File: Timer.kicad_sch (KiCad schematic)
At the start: 26 parts, among them J201 Conn_02x06_Row_Letter_First, P201 Interrupt Daisy Chain SIO, P202 Interrupt Daisy Chain CTC, P203 CONN_02X10, P204 Outputs, P205 Inputs, U201 Z8430, U202 Z8440

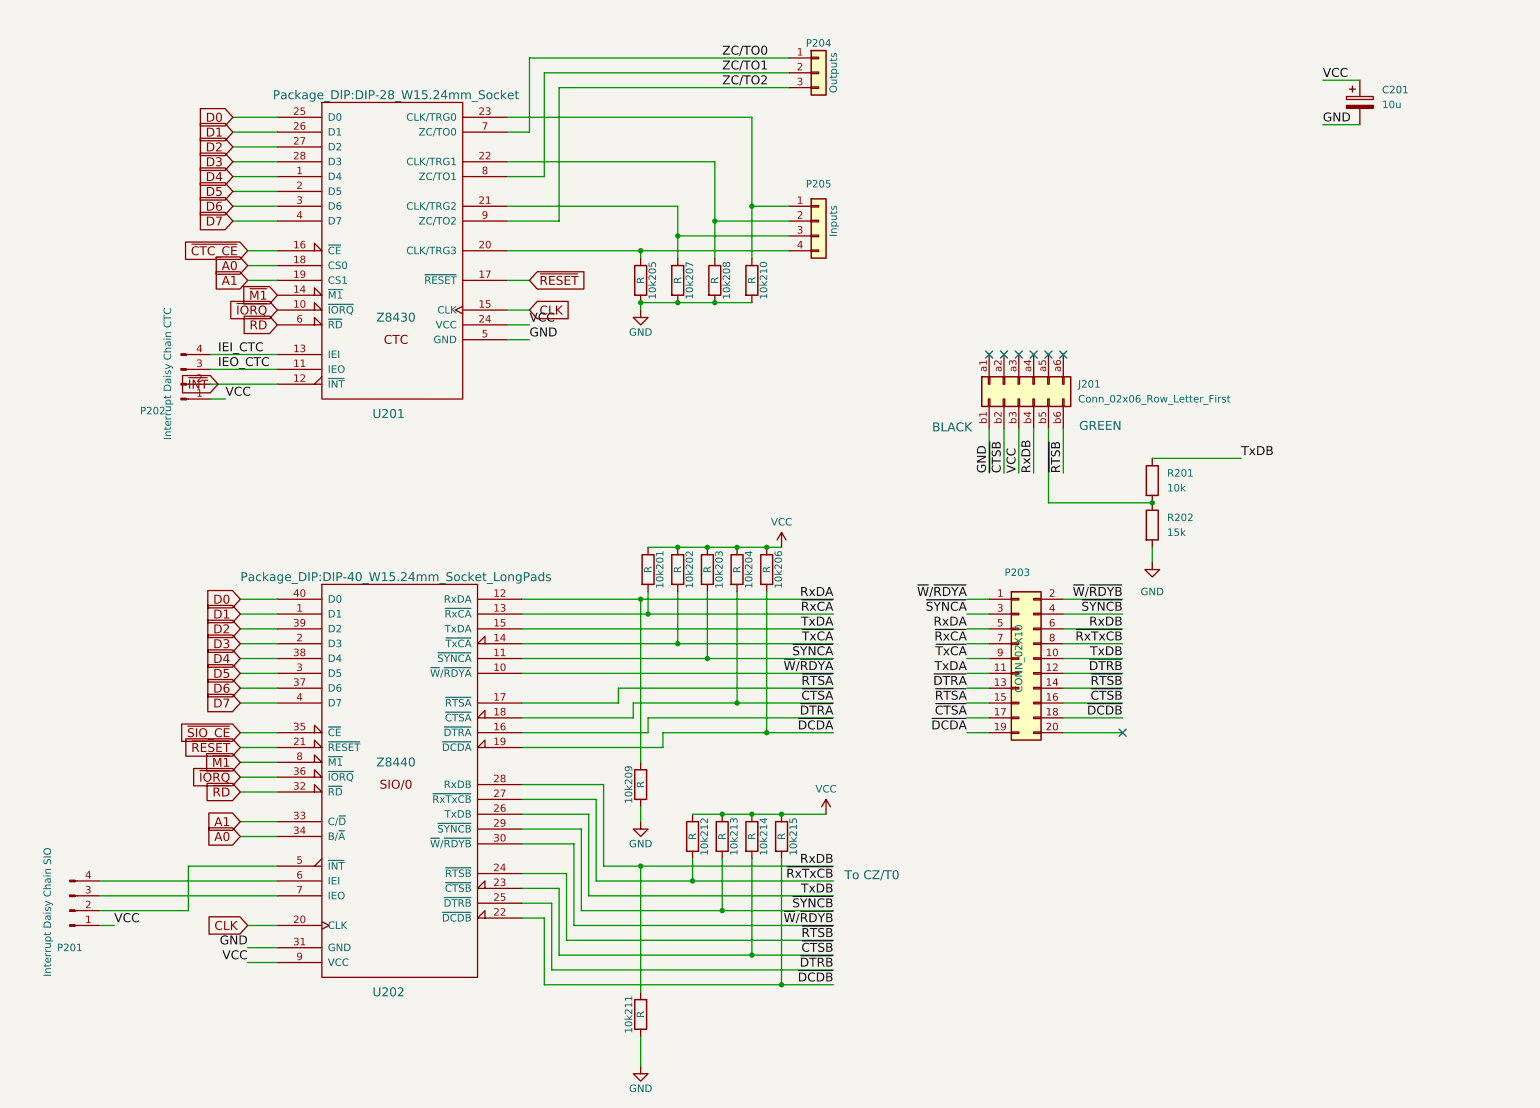
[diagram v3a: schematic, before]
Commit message: Continued layout of timer/sio board
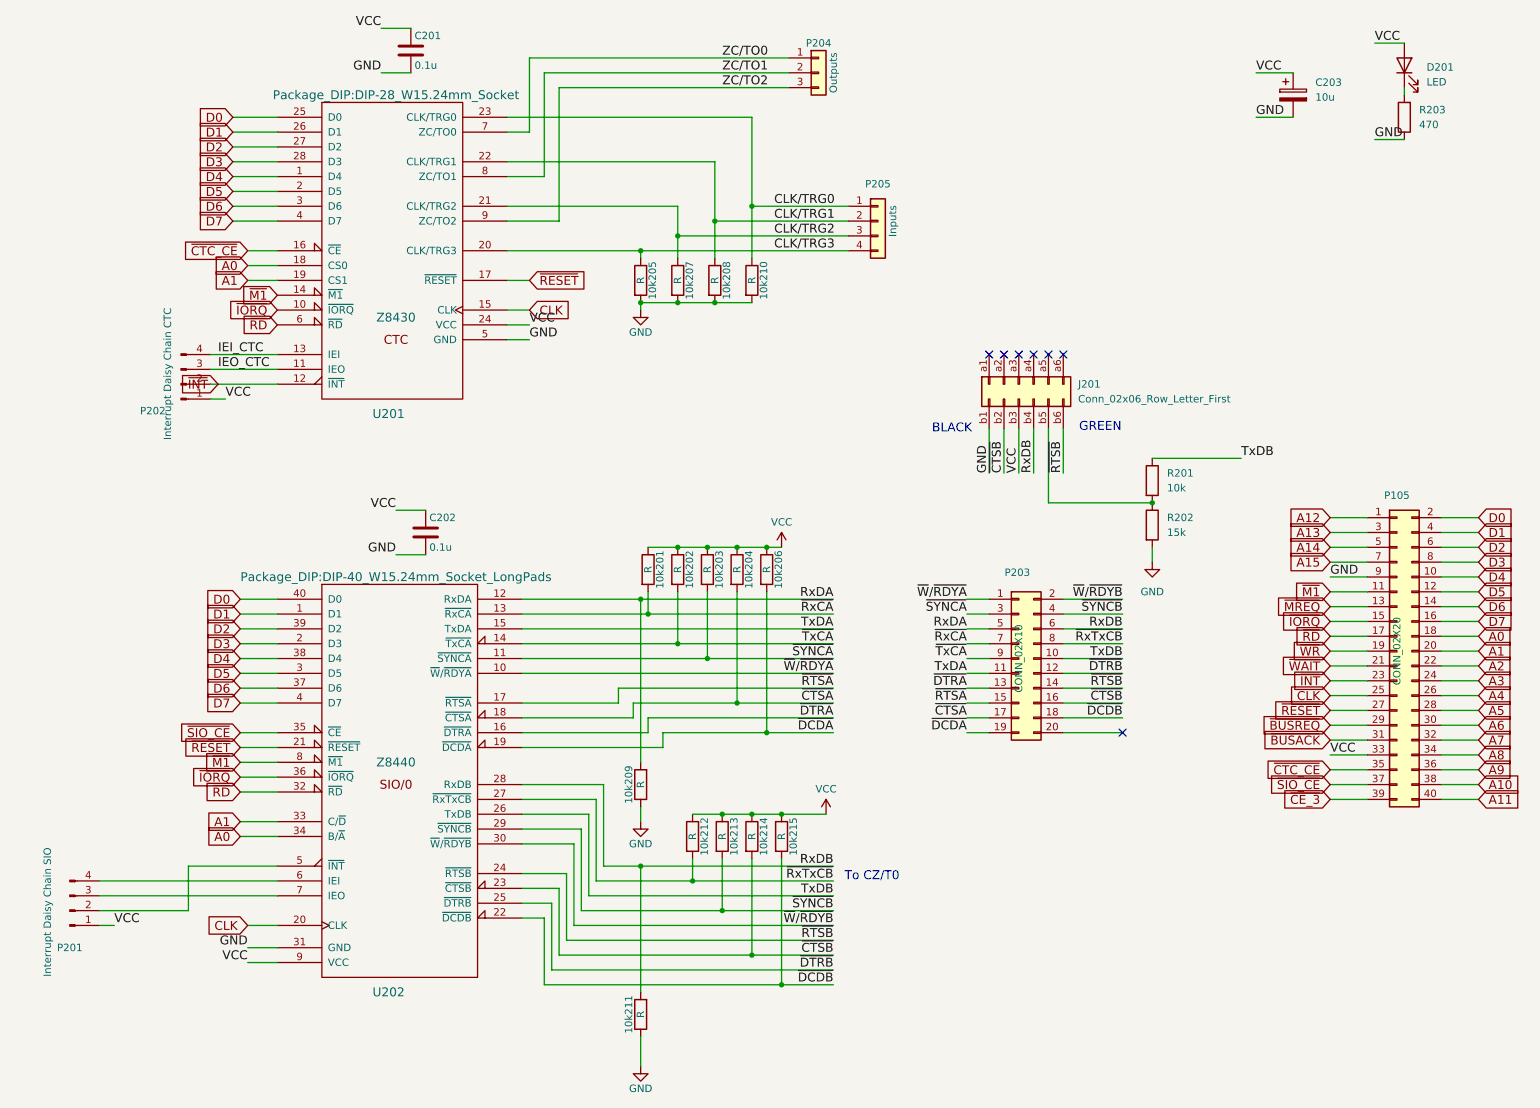
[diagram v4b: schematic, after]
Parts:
- removed C201: 10u, Capacitor_THT:CP_Radial_D10.0mm_P5.00mm, symbol Device:C_Polarized
- added C201, C202: 0.1u, Capacitor_SMD:C_0805_2012Metric_Pad1.18x1.45mm_HandSolder, symbol Device:C
- added C203: 10u, Capacitor_THT:CP_Radial_D10.0mm_P5.00mm, symbol Device:C_Polarized
- added D201: LED, LED_SMD:LED_0805_2012Metric_Pad1.15x1.40mm_HandSolder, symbol Device:LED
- added P105: CONN_02X20, Connector_PinHeader_2.54mm:PinHeader_2x20_P2.54mm_Horizontal, symbol Connector_Generic:Conn_02x20_Odd_Even
- added R203: 470, Resistor_SMD:R_0805_2012Metric_Pad1.20x1.40mm_HandSolder, symbol Device:R
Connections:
- net A0: now also P105.18 (Pin_18)
- net A1: now also P105.20 (Pin_20)
- net CLK: now also P105.25 (Pin_25)
- net D0: now also P105.2 (Pin_2)
- net D1: now also P105.4 (Pin_4)
- net D2: now also P105.6 (Pin_6)
- net D3: now also P105.8 (Pin_8)
- net D4: now also P105.10 (Pin_10)
- net D5: now also P105.12 (Pin_12)
- net D6: now also P105.14 (Pin_14)
- net D7: now also P105.16 (Pin_16)
- net GND: now also C201.2, C202.2, C203.2, P105.9 (Pin_9), R203.1
- net VCC: now also C201.1, C202.1, C203.1, D201.2 (A), P105.33 (Pin_33)
- net ~{CTC_CE}: now also P105.35 (Pin_35)
- net ~{INT}: now also P105.23 (Pin_23)
- net ~{IORQ}: now also P105.15 (Pin_15)
- net ~{M1}: now also P105.11 (Pin_11)
- net ~{RD}: now also P105.17 (Pin_17)
- net ~{RESET}: now also P105.27 (Pin_27)
- net ~{SIO_CE}: now also P105.37 (Pin_37)
- net CLK/TRG3: now reaches 10k205.1, P205.4 (Pin_4), U201.20 (CLK/TRG3)
- net CLK/TRG2: now reaches 10k207.1, P205.3 (Pin_3), U201.21 (CLK/TRG2)
- net CLK/TRG1: now reaches 10k208.1, P205.2 (Pin_2), U201.22 (CLK/TRG1)
- net CLK/TRG0: now reaches 10k210.1, P205.1 (Pin_1), U201.23 (CLK/TRG0)
- new net: D201.1 (K), R203.2
- new net A10: P105.38 (Pin_38)
- new net A11: P105.40 (Pin_40)
- new net A12: P105.1 (Pin_1)
- new net A13: P105.3 (Pin_3)
- new net A14: P105.5 (Pin_5)
- new net A15: P105.7 (Pin_7)
- new net A2: P105.22 (Pin_22)
- new net A3: P105.24 (Pin_24)
- new net A4: P105.26 (Pin_26)
- new net A5: P105.28 (Pin_28)
- new net A6: P105.30 (Pin_30)
- new net A7: P105.32 (Pin_32)
- new net A8: P105.34 (Pin_34)
- new net A9: P105.36 (Pin_36)
- new net ~{BUSACK}: P105.31 (Pin_31)
- new net ~{BUSREQ}: P105.29 (Pin_29)
- new net ~{CE_3}: P105.39 (Pin_39)
- new net ~{MREQ}: P105.13 (Pin_13)
- new net ~{WAIT}: P105.21 (Pin_21)
- new net ~{WR}: P105.19 (Pin_19)
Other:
- moved on the sheet: P205

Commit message: PCB routing almost complete
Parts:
- J201: footprint Connector_PinHeader_2.54mm:PinHeader_2x06_P2.54mm_Vertical -> Connector_PinHeader_2.54mm:PinHeader_2x06_P2.54mm_Horizontal; symbol Connector_Generic:Conn_02x06_Row_Letter_First -> Connector_Generic:Conn_02x06_Odd_Even
- P201, P202: footprint Connector_PinHeader_2.54mm:PinHeader_1x04_P2.54mm_Vertical -> Connector_PinHeader_2.54mm:PinHeader_1x03_P2.54mm_Vertical; symbol Connector:Conn_01x04_Pin -> Connector:Conn_01x03_Pin
- R201: renamed from 10k201; value R -> 10k
- R202: renamed from 10k202; value R -> 10k
- R203: renamed from 10k203; value R -> 10k
- R204: renamed from 10k204; value R -> 10k
- R205: renamed from 10k206; value R -> 10k
- R206: renamed from 10k205; value R -> 10k
- R207: renamed from 10k207; value R -> 10k
- R208: renamed from 10k208; value R -> 10k
- R209: renamed from 10k209; value R -> 10k
- R210: renamed from 10k210; value R -> 10k
- R211: renamed from 10k211; value R -> 10k
- R212: renamed from 10k212; value R -> 10k
- R213: renamed from 10k213; value R -> 10k
- R214: renamed from 10k214; value R -> 10k
- R215: renamed from 10k215; value R -> 10k
- renumbered R201 to R216, R202 to R217, R203 to R218
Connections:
- net GND: now also J201.2 (Pin_2); no longer J201.b1 (Pin_b1)
- net IEI_CTC: now also P202.2 (Pin_2); no longer P202.4 (Pin_4)
- net RxDB: now also J201.8 (Pin_8); no longer J201.b4 (Pin_b4)
- net VCC: now also J201.6 (Pin_6); no longer J201.b3 (Pin_b3)
- net ~{CTSB}: now also J201.4 (Pin_4); no longer J201.b2 (Pin_b2)
- net ~{INT}: now also U202.5 (~{INT}); no longer P202.2 (Pin_2)
- net ~{RTSB}: now also J201.12 (Pin_12); no longer J201.b6 (Pin_b6)
- net IEI_SIO: now reaches P201.2 (Pin_2)
- net IEI_SIO: now also U202.6 (IEI); no longer U202.5 (~{INT})
- net IEO_SIO: now reaches P201.3 (Pin_3), U202.7 (IEO)
- net TxDB3.3V: now reaches R216.2, R217.1
- net TxDB3.3V: now also J201.10 (Pin_10); no longer J201.b5 (Pin_b5)
- net A10: no longer names the net of P105.38 (Pin_38)
- net A11: no longer names the net of P105.40 (Pin_40)
- net A12: no longer names the net of P105.1 (Pin_1)
- net A13: no longer names the net of P105.3 (Pin_3)
- net A14: no longer names the net of P105.5 (Pin_5)
- net A15: no longer names the net of P105.7 (Pin_7)
- net A2: no longer names the net of P105.22 (Pin_22)
- net A3: no longer names the net of P105.24 (Pin_24)
- net A4: no longer names the net of P105.26 (Pin_26)
- net A5: no longer names the net of P105.28 (Pin_28)
- net A6: no longer names the net of P105.30 (Pin_30)
- net A7: no longer names the net of P105.32 (Pin_32)
- net A8: no longer names the net of P105.34 (Pin_34)
- net A9: no longer names the net of P105.36 (Pin_36)
- net ~{BUSACK}: no longer names the net of P105.31 (Pin_31)
- net ~{BUSREQ}: no longer names the net of P105.29 (Pin_29)
- net ~{CE_3}: no longer names the net of P105.39 (Pin_39)
- net ~{MREQ}: no longer names the net of P105.13 (Pin_13)
- net ~{WAIT}: no longer names the net of P105.21 (Pin_21)
- net ~{WR}: no longer names the net of P105.19 (Pin_19)
- no-connect marks 7 -> 27

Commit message: Removed serial board which has now been moved to its own project.
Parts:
- removed C201, C202: 0.1u, Capacitor_SMD:C_0805_2012Metric_Pad1.18x1.45mm_HandSolder, symbol Device:C
- removed C203: 10u, Capacitor_THT:CP_Radial_D10.0mm_P5.00mm, symbol Device:C_Polarized
- removed D201: LED, LED_SMD:LED_0805_2012Metric_Pad1.15x1.40mm_HandSolder, symbol Device:LED
- removed J201: Conn_02x06_Row_Letter_First, Connector_PinHeader_2.54mm:PinHeader_2x06_P2.54mm_Horizontal, symbol Connector_Generic:Conn_02x06_Odd_Even
- removed P105: CONN_02X20, Connector_PinHeader_2.54mm:PinHeader_2x20_P2.54mm_Horizontal, symbol Connector_Generic:Conn_02x20_Odd_Even
- removed P201: Interrupt Daisy Chain SIO, Connector_PinHeader_2.54mm:PinHeader_1x03_P2.54mm_Vertical, symbol Connector:Conn_01x03_Pin
- removed P202: Interrupt Daisy Chain CTC, Connector_PinHeader_2.54mm:PinHeader_1x03_P2.54mm_Vertical, symbol Connector:Conn_01x03_Pin
- removed P203: CONN_02X10, Connector_PinHeader_2.54mm:PinHeader_2x10_P2.54mm_Vertical, symbol Connector_Generic:Conn_02x10_Odd_Even
- removed P204: Outputs, Connector_PinHeader_2.54mm:PinHeader_1x03_P2.54mm_Vertical, symbol Connector_Generic:Conn_01x03
- removed P205: Inputs, Connector_PinHeader_2.54mm:PinHeader_1x04_P2.54mm_Vertical, symbol Connector_Generic:Conn_01x04
- removed R201, R202, R203, R204, R205, R206, R207, R208, R209, R210, R211, R212, R213, R214, R215, R216: 10k, Resistor_SMD:R_0805_2012Metric_Pad1.20x1.40mm_HandSolder, symbol Device:R
- removed R217: 15k, Resistor_SMD:R_0805_2012Metric_Pad1.20x1.40mm_HandSolder, symbol Device:R
- removed R218: 470, Resistor_SMD:R_0805_2012Metric_Pad1.20x1.40mm_HandSolder, symbol Device:R
- removed U201: Z8430, Package_DIP:DIP-28_W15.24mm_Socket, symbol z80-ownSymbols:Z8430
- removed U202: Z8440, Package_DIP:DIP-40_W15.24mm_Socket_LongPads, symbol z80-ownSymbols:Z8440
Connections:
- no-connect marks 27 -> 0
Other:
- note removed: "BLACK"
- note removed: "GREEN"
- note removed: "To CZ/T0"
